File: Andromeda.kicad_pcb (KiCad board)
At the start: 2 copper layers, 30 parts, among them J1 Barrel_Jack, J2 USB_C_Receptacle_USB2.0, M1 Motor_DC, SW1 Reset, SW2 Boot, SW4 SW_DIP_x01, U1 ESP32-S2-SOLO, U2 DRV8871DDA, U3 AP2127K-3.3

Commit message: begin layout
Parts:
- removed C19: 47uF, Capacitor_SMD:C_0805_2012Metric
- removed D2: LED, Diode_SMD:D_1206_3216Metric
- removed M1: Motor_DC, Connector_Wire:SolderWire-0.75sqmm_1x02_P7mm_D1.25mm_OD3.5mm
- removed SW4: SW_DIP_x01, Connector_Wire:SolderWire-2.5sqmm_1x02_P7.2mm_D2.4mm_OD3.6mm
- added C10: 0.1uF, Capacitor_SMD:C_0805_2012Metric, F.Cu at (180.7, 137.0)
- added C11: 10uF, Capacitor_SMD:C_0805_2012Metric, F.Cu at (27.9, 24.1)
- added C12: 0.1uF, Capacitor_SMD:C_0805_2012Metric, F.Cu at (27.9, 30.0)
- added C13: 22uF, Capacitor_SMD:C_0805_2012Metric, F.Cu at (29.2, 38.1)
- added C14: 22uF, Capacitor_SMD:C_0805_2012Metric, F.Cu at (39.0, 44.5)
- added C15: 0.1uF, Capacitor_SMD:C_0805_2012Metric, F.Cu at (176.5, 102.2)
- added C16: 0.1uF, Capacitor_SMD:C_0805_2012Metric, F.Cu at (180.9, 102.2)
- added C18: 0.1uF, Capacitor_SMD:C_0805_2012Metric, F.Cu at (76.2, 189.2)
- added C7: 0.1uF, Capacitor_SMD:C_0805_2012Metric, F.Cu at (117.2, 174.0)
- added C8: 0.1uF, Capacitor_SMD:C_0805_2012Metric, F.Cu at (64.8, 177.8)
- added C9: 0.1uF, Capacitor_SMD:C_0805_2012Metric, F.Cu at (176.2, 137.0)
- added F2: Fuse_Small, Fuse:Fuse_0805_2012Metric, F.Cu at (180.0, 59.7)
- added J10: RJ45, Connector_RJ:RJ45_Amphenol_54602-x08_Horizontal, F.Cu at (238.7, 130.1)
- added J11: Conn_01x08_Pin, Connector_PinHeader_2.54mm:PinHeader_2x08_P2.54mm_Vertical, F.Cu at (16.3, 118.6)
- added J12: RJ45, Connector_RJ:RJ45_Amphenol_54602-x08_Horizontal, F.Cu at (238.7, 112.4)
- added J13: RJ45, Connector_RJ:RJ45_Amphenol_54602-x08_Horizontal, F.Cu at (238.7, 94.7)
- added J3: RJ45, Connector_RJ:RJ45_Amphenol_54602-x08_Horizontal, F.Cu at (167.6, 85.9)
- added J4: RJ45, Connector_RJ:RJ45_Amphenol_54602-x08_Horizontal, F.Cu at (167.6, 103.6)
- added J5: RJ45, Connector_RJ:RJ45_Amphenol_54602-x08_Horizontal, F.Cu at (167.6, 121.3)
- added J6: RJ45, Connector_RJ:RJ45_Amphenol_54602-x08_Horizontal, F.Cu at (167.6, 138.9)
- added J7: RJ45, Connector_RJ:RJ45_Amphenol_54602-x08_Horizontal, F.Cu at (210.8, 137.2)
- added J8: RJ45, Connector_RJ:RJ45_Amphenol_54602-x08_Horizontal, F.Cu at (191.0, 137.2)
- added J9: RJ45, Connector_RJ:RJ45_Amphenol_54602-x08_Horizontal, F.Cu at (238.7, 147.8)
- added L1: 4.7uH, Inductor_THT:L_Radial_D9.5mm_P5.00mm_Fastron_07HVP, F.Cu at (47.0, 34.3)
- added R10: 1K, Resistor_SMD:R_0805_2012Metric, F.Cu at (81.6, 172.7)
- added R11: 1K, Resistor_SMD:R_0805_2012Metric, F.Cu at (180.9, 106.0)
- added R14: 1K, Resistor_SMD:R_0805_2012Metric, F.Cu at (68.9, 185.4)
- added R15: 1K, Resistor_SMD:R_0805_2012Metric, F.Cu at (175.9, 146.1)
- added R16: 1K, Resistor_SMD:R_0805_2012Metric, F.Cu at (175.9, 148.6)
- added R17: 1K, Resistor_SMD:R_0805_2012Metric, F.Cu at (176.5, 112.4)
- added R18: 1K, Resistor_SMD:R_0805_2012Metric, F.Cu at (176.5, 114.9)
- added R19: 1K, Resistor_SMD:R_0805_2012Metric, F.Cu at (212.4, 128.9)
- added R20: 1K, Resistor_SMD:R_0805_2012Metric, F.Cu at (220.3, 129.5)
- added R21: 1K, Resistor_SMD:R_0805_2012Metric, F.Cu at (200.3, 129.5)
- added R22: 1K, Resistor_SMD:R_0805_2012Metric, F.Cu at (193.7, 128.9)
- added R23: 1K, Resistor_SMD:R_0805_2012Metric, F.Cu at (229.9, 142.2)
- added R24: 1K, Resistor_SMD:R_0805_2012Metric, F.Cu at (229.9, 137.8)
- added R25: 1K, Resistor_SMD:R_0805_2012Metric, F.Cu at (229.5, 125.1)
- added R26: 1K, Resistor_SMD:R_0805_2012Metric, F.Cu at (229.2, 120.0)
- added R27: 1K, Resistor_SMD:R_0805_2012Metric, F.Cu at (230.1, 104.1)
- added R28: 1K, Resistor_SMD:R_0805_2012Metric, F.Cu at (229.9, 108.6)
- added R29: 1K, Resistor_SMD:R_0805_2012Metric, F.Cu at (229.2, 90.2)
- added R30: 1K, Resistor_SMD:R_0805_2012Metric, F.Cu at (229.2, 85.1)
- added R31: 1K, Resistor_SMD:R_0805_2012Metric, F.Cu at (29.4, 115.6)
- added R32: 1K, Resistor_SMD:R_0805_2012Metric, F.Cu at (29.2, 123.2)
- added R33: 1K, Resistor_SMD:R_0805_2012Metric, F.Cu at (32.7, 140.1)
- added R34: 1K, Resistor_SMD:R_0805_2012Metric, F.Cu at (27.9, 132.1)
- added R5: 1K, Resistor_SMD:R_0805_2012Metric, F.Cu at (116.3, 179.1)
- added R6: 1K, Resistor_SMD:R_0805_2012Metric, F.Cu at (180.6, 140.9)
- added R7: 1K, Resistor_SMD:R_0805_2012Metric, F.Cu at (43.5, 22.9)
- added R8: 1K, Resistor_SMD:R_0805_2012Metric, F.Cu at (110.5, 171.4)
- added SW3: SW_Nidec_CAS-120A1, Button_Switch_SMD:Nidec_Copal_CAS-120A, F.Cu at (219.1, 43.8)
- added U4: DRV8212DSGR, DRV8870DDA:WSON_212DSGR_TEX, F.Cu at (176.3, 140.9)
- added U5: AP63205WU, Package_TO_SOT_SMD:TSOT-23-6, F.Cu at (36.8, 33.0)
- added U6: DRV8212DSGR, DRV8870DDA:WSON_212DSGR_TEX, F.Cu at (126.0, 175.8)
- added U7: DRV8212DSGR, DRV8870DDA:WSON_212DSGR_TEX, F.Cu at (78.7, 181.6)
- C2, C5: footprint Capacitor_SMD:C_0603_1608Metric -> Capacitor_SMD:C_0805_2012Metric
- R3: value 150 -> 1K; footprint Resistor_SMD:R_0603_1608Metric -> Resistor_SMD:R_0805_2012Metric
- R4: value 30k -> 1K
- R9: footprint Resistor_SMD:R_0603_1608Metric -> Resistor_SMD:R_0805_2012Metric
- U2: value DRV8871DDA -> DRV8212DSGR; footprint Package_SO:Texas_HTSOP-8-1EP_3.9x4.9mm_P1.27mm_EP2.95x4.9mm_Mask2.4x3.1mm_ThermalVias -> DRV8870DDA:WSON_212DSGR_TEX
- moved J1 123.3 mm to (242.8, 62.9), turned to 90 degrees
- moved R4 122.3 mm to (72.4, 174.0)
- moved U1 118.3 mm to (208.4, 90.6)
- moved D3 100.5 mm to (35.3, 72.4)
- moved TP2 97.8 mm to (21.0, 49.8)
- moved TP3 97.8 mm to (21.0, 55.9)
- moved C17 96.1 mm to (117.2, 167.6)
- moved F1 93.6 mm to (227.8, 43.8)
- moved R3 92.8 mm to (109.6, 177.8)
- moved R9 91.6 mm to (27.9, 72.4)
- moved C5 60.0 mm to (118.4, 22.9)
- moved C6 56.3 mm to (101.9, 21.6)
- moved D4 55.2 mm to (170.2, 59.7), turned to 180 degrees
- moved R2 54.0 mm to (84.2, 82.5)
- moved C1 50.8 mm to (82.5, 74.9)
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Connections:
- C17 pad 1: +12V -> +3.3V
- D4 pad 1: +5V -> Net-(D4-K)
- F1 pad 1: Net-(F1-Pad1) -> Net-(SW3-C)
- J1 pad 1: Net-(F1-Pad1) -> Net-(SW3-B)
- R3 pad 1: +5V -> Net-(U6-MODE)
- R3 pad 2: Net-(D2-A) -> GND
- R4 pad 1: Net-(U2-ILIM) -> Net-(U7-MODE)
- U1 pad 10: unconnected-(U1-GPIO17/U1TXD/ADC2_CH6/DAC_1-Pad10) -> GPIO17
- U1 pad 11: unconnected-(U1-GPIO18/U1RXD/ADC2_CH7/DAC_2/CLK_OUT3-Pad11) -> GPIO18
- U1 pad 12: unconnected-(U1-GPIO8/TOUCH8/ADC1_CH7-Pad12) -> GPIO8
- U1 pad 15: unconnected-(U1-GPIO3/TOUCH3/ADC1_CH2-Pad15) -> GPIO3
- U1 pad 22: unconnected-(U1-GPIO14/TOUCH14/ADC2_CH3/FSPIWP/FSPIDQS-Pad22) -> GPIO14
- U1 pad 26: unconnected-(U1-GPIO45-Pad26) -> GPIO45
- U1 pad 30: unconnected-(U1-SPIDQS/GPIO37/FSPIQ-Pad30) -> GPIO37
- U1 pad 31: unconnected-(U1-GPIO38/FSPIWP-Pad31) -> GPIO38
- U1 pad 32: unconnected-(U1-MTCK/GPIO39/CLK_OUT3-Pad32) -> GPIO39
- U1 pad 33: unconnected-(U1-MTDO/GPIO40/CLK_OUT2-Pad33) -> GPIO40
- U1 pad 34: unconnected-(U1-MTDI/GPIO41/CLK_OUT1-Pad34) -> GPIO41
- U1 pad 35: unconnected-(U1-MTMS/GPIO42-Pad35) -> GPIO42
- U1 pad 36: unconnected-(U1-U0RXD/GPIO44/CLK_OUT2-Pad36) -> GPIO44
- U1 pad 37: unconnected-(U1-U0TXD/GPIO43/CLK_OUT1-Pad37) -> GPIO43
- U1 pad 38: unconnected-(U1-GPIO2/TOUCH2/ADC1_CH1-Pad38) -> GPIO2
- U1 pad 39: unconnected-(U1-GPIO1/TOUCH1/ADC1_CH0-Pad39) -> GPIO1
- U1 pad 5: unconnected-(U1-GPIO5/TOUCH5/ADC1_CH4-Pad5) -> GPIO5
- U1 pad 6: unconnected-(U1-GPIO6/TOUCH6/ADC1_CH5-Pad6) -> GPIO6
- U1 pad 7: unconnected-(U1-GPIO7/TOUCH7/ADC1_CH6-Pad7) -> GPIO7
- U1 pad 8: unconnected-(U1-GPIO15/U0RTS/ADC2_CH4/XTAL_32K_P-Pad8) -> GPIO15
- U1 pad 9: unconnected-(U1-GPIO16/U0CTS/ADC2_CH5/XTAL_32K_N-Pad9) -> GPIO16
- U2 pad 1: GND -> +6V
- U2 pad 2: GPIO36 -> Net-(U2-OUT1)
- U2 pad 3: GPIO35 -> Net-(U2-OUT2)
- U2 pad 4: Net-(U2-ILIM) -> GND
- U2 pad 5: +12V -> GPIO40
- U2 pad 6: Net-(U2-OUT1) -> GPIO39
- U2 pad 7: GND -> Net-(U2-MODE)
- U2 pad 8: Net-(M1--) -> +3.3V
- U2 pad 9: GND -> (no net)
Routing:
- net Net-(U4-OUT1): track 0.00 -> 9.44 mm
- net Net-(U2-OUT1): track 0.00 -> 9.02 mm
- net Net-(J4-Pad7): track 0.00 -> 8.48 mm
- net +3.3V: track 0.00 -> 8.42 mm
- net Net-(J6-Pad7): track 0.00 -> 7.55 mm
- net Net-(J4-Pad8): track 0.00 -> 6.46 mm
- net +6V: track 0.00 -> 6.40 mm
- net Net-(U2-OUT2): track 0.00 -> 6.16 mm
- net Net-(U4-OUT2): track 0.00 -> 5.86 mm
- net Net-(J6-Pad8): track 0.00 -> 5.12 mm
- net Net-(U2-MODE): track 0.00 -> 2.58 mm
- net Net-(U4-MODE): track 0.00 -> 2.54 mm
- added copper zone on B.Cu, net GND
- added copper zone on F.Cu, net GND
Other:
- board outline added: 101.6 x 101.6 mm

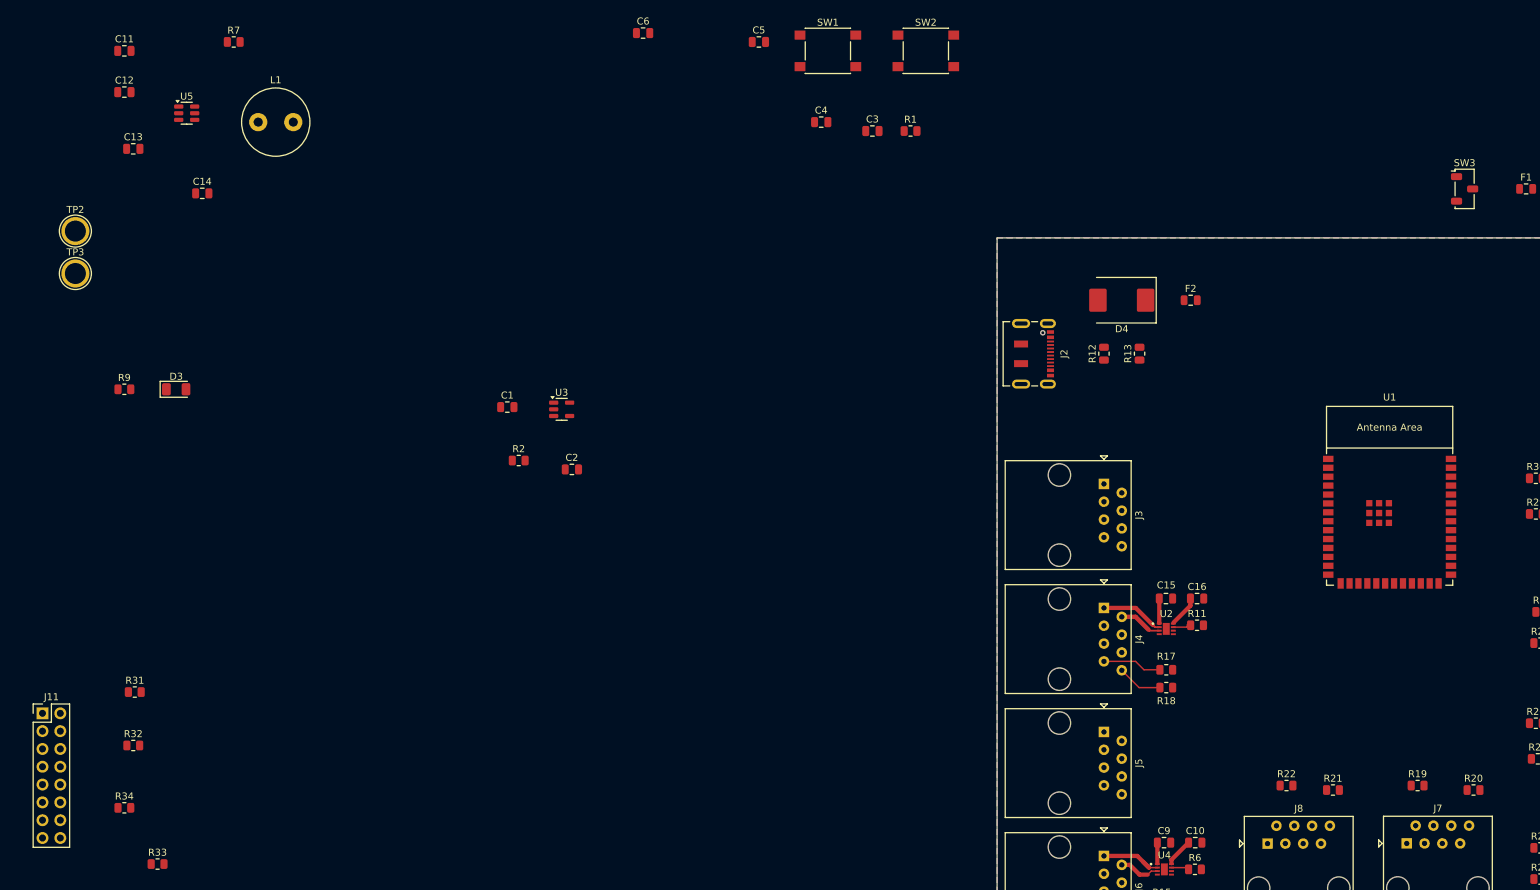
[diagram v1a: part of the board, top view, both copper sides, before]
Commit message: Switch to 5V, Add Gyro, GPIO extender
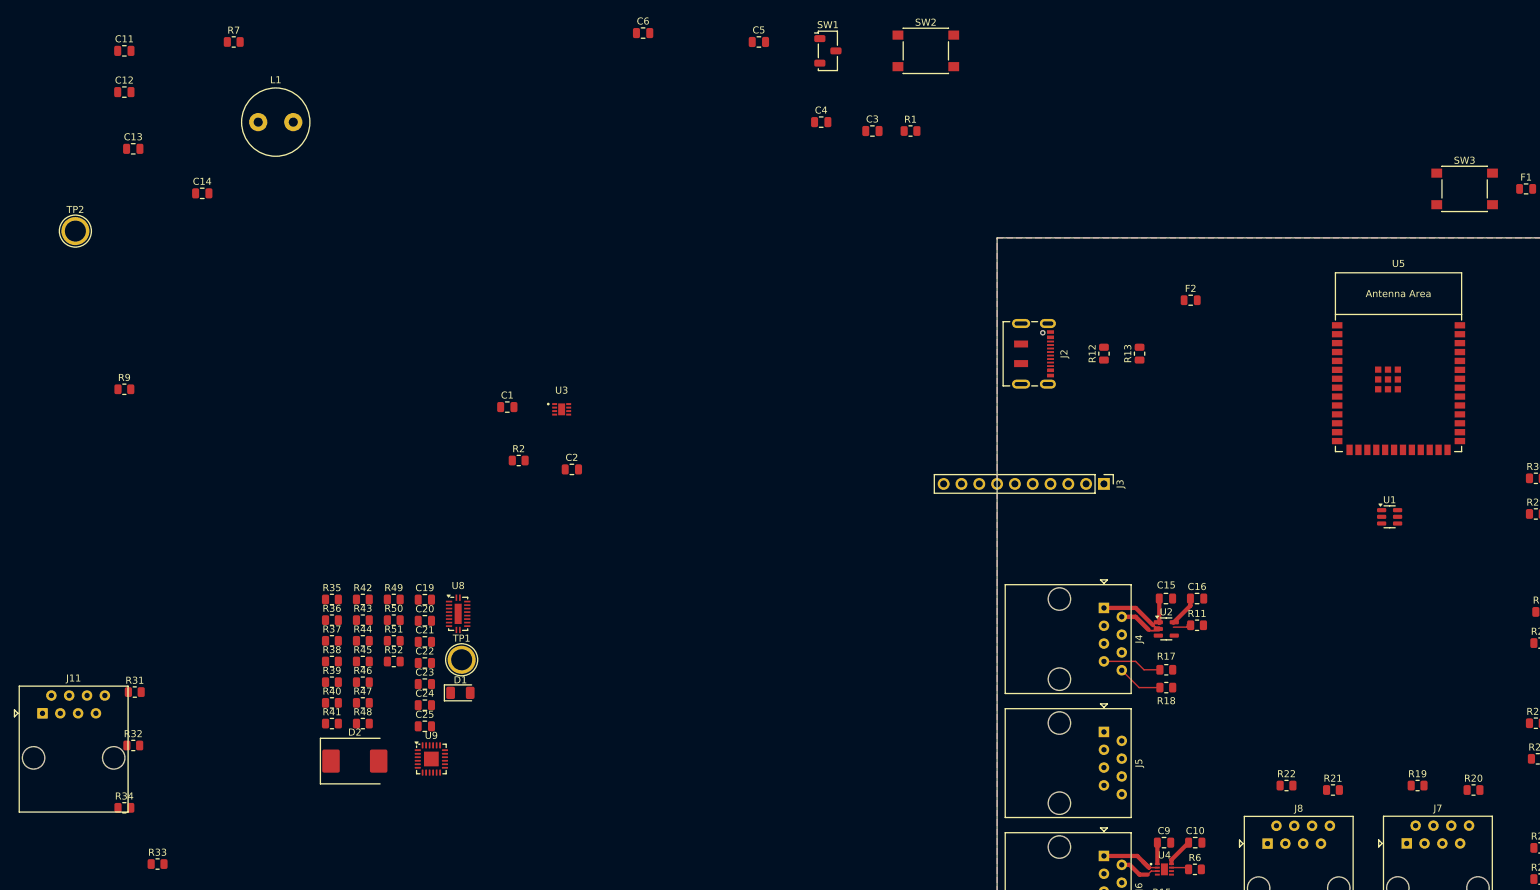
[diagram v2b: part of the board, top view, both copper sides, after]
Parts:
- removed D3: LED, Diode_SMD:D_1206_3216Metric
- removed D4: D_Schottky, Diode_SMD:D_SMC
- removed TP3: TestPoint, TestPoint:TestPoint_Plated_Hole_D3.0mm
- added C19: .1uF, Capacitor_SMD:C_0805_2012Metric, F.Cu at (70.8, 102.4)
- added C20: .1uF, Capacitor_SMD:C_0805_2012Metric, F.Cu at (70.8, 105.4)
- added C21: .1uF, Capacitor_SMD:C_0805_2012Metric, F.Cu at (70.8, 108.4)
- added C22: 10nF, Capacitor_SMD:C_0805_2012Metric, F.Cu at (70.8, 111.4)
- added C23: .1uF, Capacitor_SMD:C_0805_2012Metric, F.Cu at (70.8, 114.4)
- added C24: 0.1uF, Capacitor_SMD:C_0805_2012Metric, F.Cu at (70.8, 117.4)
- added C25: 2.2uF, Capacitor_SMD:C_0805_2012Metric, F.Cu at (70.8, 120.5)
- added D1: LED, Diode_SMD:D_1206_3216Metric, F.Cu at (75.9, 115.7)
- added D2: D_Schottky, Diode_SMD:D_SMC, F.Cu at (60.8, 125.4)
- added R35: 20K, Resistor_SMD:R_0805_2012Metric, F.Cu at (57.5, 102.4)
- added R36: 10K, Resistor_SMD:R_0805_2012Metric, F.Cu at (57.5, 105.3)
- added R37: 10K, Resistor_SMD:R_0805_2012Metric, F.Cu at (57.5, 108.3)
- added R38: 10K, Resistor_SMD:R_0805_2012Metric, F.Cu at (57.5, 111.2)
- added R39: 10K, Resistor_SMD:R_0805_2012Metric, F.Cu at (57.5, 114.2)
- added R40: 1K, Resistor_SMD:R_0805_2012Metric, F.Cu at (57.5, 117.1)
- added R41: 1K, Resistor_SMD:R_0805_2012Metric, F.Cu at (57.5, 120.1)
- added R42: 10K, Resistor_SMD:R_0805_2012Metric, F.Cu at (62.0, 102.4)
- added R43: 20K, Resistor_SMD:R_0805_2012Metric, F.Cu at (62.0, 105.3)
- added R44: 10K, Resistor_SMD:R_0805_2012Metric, F.Cu at (62.0, 108.3)
- added R45: 10K, Resistor_SMD:R_0805_2012Metric, F.Cu at (62.0, 111.2)
- added R46: 10K, Resistor_SMD:R_0805_2012Metric, F.Cu at (62.0, 114.2)
- added R47: 10K, Resistor_SMD:R_0805_2012Metric, F.Cu at (62.0, 117.1)
- added R48: 1K, Resistor_SMD:R_0805_2012Metric, F.Cu at (62.0, 120.1)
- added R49: 10K, Resistor_SMD:R_0805_2012Metric, F.Cu at (66.4, 102.4)
- added R50: 1K, Resistor_SMD:R_0805_2012Metric, F.Cu at (66.4, 105.3)
- added R51: 10K, Resistor_SMD:R_0805_2012Metric, F.Cu at (66.4, 108.3)
- added R52: 20K, Resistor_SMD:R_0805_2012Metric, F.Cu at (66.4, 111.2)
- added TP1: TestPoint, TestPoint:TestPoint_Plated_Hole_D3.0mm, F.Cu at (76.0, 111.0)
- added U8: FXMA108, Package_DFN_QFN:WQFN-20-1EP_2.5x4.5mm_P0.5mm_EP1x2.9mm, F.Cu at (75.5, 104.4)
- added U9: PCAL6416AHF, Package_DFN_QFN:HVQFN-24-1EP_4x4mm_P0.5mm_EP2.1x2.1mm, F.Cu at (71.7, 125.1)
- C1: value 1uF -> 10uF
- C10: value 0.1uF -> 1uF
- C11: value 10uF -> .1uF
- C13, C14: value 22uF -> 0.1uF
- C16, C7: value 0.1uF -> .1uF
- C3: value .1uF -> 1uF
- C4: value .1uF -> 0.1uF
- C5: value 1uF -> 22uF
- C6: value .1uF -> 22uF
- J11: value Conn_01x08_Pin -> RJ45; footprint Connector_PinHeader_2.54mm:PinHeader_2x08_P2.54mm_Vertical -> Connector_RJ:RJ45_Amphenol_54602-x08_Horizontal
- J3: value RJ45 -> Conn_01x10_Pin; footprint Connector_RJ:RJ45_Amphenol_54602-x08_Horizontal -> Connector_PinHeader_2.54mm:PinHeader_1x10_P2.54mm_Vertical
- R1: value 10k -> 60
- R12, R13: value 5.1k -> 1K
- R2: value 3M -> 1K
- R23, R25, R32, R34: value 1K -> 10K
- R24, R26, R33: value 1K -> 20K
- R3: value 1K -> 3M
- R4, R5: value 1K -> 5.1k
- R6: value 1K -> 10k
- R9: value 60 -> 1K
- SW1: value Reset -> SW_Nidec_CAS-120A1; footprint Button_Switch_SMD:SW_Push_1P1T_NO_6x6mm_H9.5mm -> Button_Switch_SMD:Nidec_Copal_CAS-120A
- SW2: value Boot -> Reset
- SW3: value SW_Nidec_CAS-120A1 -> Boot; footprint Button_Switch_SMD:Nidec_Copal_CAS-120A -> Button_Switch_SMD:SW_Push_1P1T_NO_6x6mm_H9.5mm
- U1: value ESP32-S2-SOLO -> AP63205WU; footprint PCM_Espressif:ESP32-S2-SOLO -> Package_TO_SOT_SMD:TSOT-23-6
- U2: value DRV8212DSGR -> AP2127K-3.3; footprint DRV8870DDA:WSON_212DSGR_TEX -> Package_TO_SOT_SMD:SOT-23-5
- U3: value AP2127K-3.3 -> DRV8212DSGR; footprint Package_TO_SOT_SMD:SOT-23-5 -> DRV8870DDA:WSON_212DSGR_TEX
- U5: value AP63205WU -> ESP32-S3-WROOM-1; footprint Package_TO_SOT_SMD:TSOT-23-6 -> PCM_Espressif:ESP32-S3-WROOM-1
- moved U5 177.1 mm to (209.7, 71.5)
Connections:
- C10 pad 1: +3.3V -> GND
- C10 pad 2: GND -> +3.3V
- C11 pad 1: +6V -> GND
- C11 pad 2: GND -> +3.3V
- C12 pad 1: Net-(U5-BST) -> +3.3V
- C12 pad 2: Net-(U5-SW) -> GND
- C13 pad 1: +5V -> +3.3V
- C14 pad 1: +5V -> +6V
- C16 pad 1: +3.3V -> Net-(U5-GPIO0/BOOT)
- C2 pad 1: +3.3V -> +6V
- C3 pad 1: GND -> +3.3V
- C3 pad 2: Net-(U1-EN) -> GND
- C4 pad 1: Net-(U1-GPIO0) -> Net-(U1-BST)
- C4 pad 2: GND -> Net-(U1-SW)
- C5 pad 1: GND -> +5V
- C5 pad 2: +3.3V -> GND
- C6 pad 1: GND -> +5V
- C6 pad 2: +3.3V -> GND
- C7 pad 1: +6V -> GND
- C7 pad 2: GND -> Net-(U5-EN)
- F1 pad 1: Net-(SW3-C) -> Net-(SW1-C)
- J10 pad 4: unconnected-(J10-Pad4) -> +5V
- J10 pad 5: +3.3V -> GND
- J10 pad 6: GND -> Net-(J10-Pad6)
- J11 pad 1: Net-(J11-Pin_1) -> unconnected-(J11-Pad1)
- J11 pad 2: Net-(J11-Pin_2) -> unconnected-(J11-Pad2)
- J11 pad 3: Net-(J11-Pin_3) -> unconnected-(J11-Pad3)
- J11 pad 4: Net-(J11-Pin_4) -> +5V
- J11 pad 5: +3.3V -> GND
- J11 pad 6: +3.3V -> Net-(J11-Pad6)
- J11 pad 7: +5V -> Net-(J11-Pad7)
- J11 pad 8: GND -> Net-(J11-Pad8)
- J12 pad 4: unconnected-(J12-Pad4) -> +5V
- J12 pad 5: +3.3V -> GND
- J12 pad 6: GND -> Net-(J12-Pad6)
- J13 pad 4: unconnected-(J13-Pad4) -> +5V
- J13 pad 5: +3.3V -> GND
- J13 pad 6: GND -> Net-(J13-Pad6)
- J3 pad 1: Net-(U6-OUT1) -> GPIO7
- J3 pad 2: Net-(U6-OUT2) -> GPIO8
- J3 pad 3: unconnected-(J3-Pad3) -> GPIO9
- J3 pad 4: +6V -> GPIO10
- J3 pad 5: +3.3V -> GPIO11
- J3 pad 6: GND -> GPIO12
- J3 pad 7: Net-(J3-Pad7) -> GPIO13
- J3 pad 8: Net-(J3-Pad8) -> GPIO14
- J4 pad 1: Net-(U2-OUT1) -> Net-(U3-OUT1)
- J4 pad 2: Net-(U2-OUT2) -> Net-(U3-OUT2)
- J4 pad 3: unconnected-(J4-Pad3) -> +6V
- J4 pad 4: +6V -> +5V
- J4 pad 5: +3.3V -> GND
- J4 pad 6: GND -> Net-(J4-Pad6)
- J4 pad 8: Net-(J4-Pad8) -> unconnected-(J4-Pad8)
- J5 pad 1: Net-(U7-OUT1) -> Net-(U4-OUT1)
- J5 pad 2: Net-(U7-OUT2) -> Net-(U4-OUT2)
- J5 pad 3: unconnected-(J5-Pad3) -> +6V
- J5 pad 4: +6V -> +5V
- J5 pad 5: +3.3V -> GND
- J5 pad 6: GND -> Net-(J5-Pad6)
- J5 pad 8: Net-(J5-Pad8) -> unconnected-(J5-Pad8)
- J6 pad 1: Net-(U4-OUT1) -> Net-(U6-OUT1)
- J6 pad 2: Net-(U4-OUT2) -> Net-(U6-OUT2)
- J6 pad 3: unconnected-(J6-Pad3) -> +6V
- J6 pad 4: +6V -> +5V
- J6 pad 5: +3.3V -> GND
- J6 pad 6: GND -> Net-(J6-Pad6)
- J6 pad 8: Net-(J6-Pad8) -> unconnected-(J6-Pad8)
- J7 pad 1: unconnected-(J7-Pad1) -> Net-(U7-OUT1)
- J7 pad 2: unconnected-(J7-Pad2) -> Net-(U7-OUT2)
- J7 pad 3: unconnected-(J7-Pad3) -> +6V
- J7 pad 4: unconnected-(J7-Pad4) -> +5V
- J7 pad 5: +3.3V -> GND
- J7 pad 6: GND -> Net-(J7-Pad6)
- J7 pad 8: Net-(J7-Pad8) -> unconnected-(J7-Pad8)
- J8 pad 4: unconnected-(J8-Pad4) -> +5V
- J8 pad 5: +3.3V -> GND
- J8 pad 6: GND -> Net-(J8-Pad6)
- J9 pad 4: unconnected-(J9-Pad4) -> +5V
- J9 pad 5: +3.3V -> GND
- J9 pad 6: GND -> Net-(J9-Pad6)
- L1 pad 1: Net-(U5-BST) -> Net-(U1-BST)
- R1 pad 2: Net-(U1-EN) -> Net-(D1-A)
- R10 pad 2: GPIO34 -> ENC3B
- R11 pad 1: Net-(U2-MODE) -> Net-(U3-MODE)
- R12 pad 1: Net-(J2-CC2) -> Net-(U4-MODE)
- R13 pad 1: Net-(J2-CC1) -> Net-(J6-Pad6)
- R13 pad 2: GND -> ENC2A
- R14 pad 1: Net-(J5-Pad8) -> Net-(J6-Pad7)
- R14 pad 2: GPIO35 -> ENC2B
- R15 pad 1: Net-(J6-Pad7) -> Net-(J7-Pad6)
- R15 pad 2: GPIO36 -> ENC4A
- R16 pad 1: Net-(J6-Pad8) -> Net-(J7-Pad7)
- R16 pad 2: GPIO45 -> ENC4B
- R17 pad 1: Net-(J4-Pad7) -> Net-(J8-Pad6)
- R17 pad 2: GPIO21 -> EXP10
- R18 pad 1: Net-(J4-Pad8) -> Net-(J8-Pad7)
- R18 pad 2: GPIO33 -> EXP11
- R19 pad 1: Net-(J7-Pad7) -> Net-(U6-MODE)
- R19 pad 2: GPIO1 -> GND
- R2 pad 1: GND -> +6V
- R2 pad 2: Net-(U3-EN) -> Net-(U1-EN)
- R20 pad 1: Net-(J7-Pad8) -> Net-(U7-MODE)
- R20 pad 2: GPIO2 -> GND
- R21 pad 1: Net-(J8-Pad7) -> Net-(J9-Pad6)
- R21 pad 2: GPIO3 -> B0
- R22 pad 1: Net-(J8-Pad8) -> Net-(J9-Pad7)
- R22 pad 2: GPIO4 -> B1
- R23 pad 1: Net-(J9-Pad7) -> Net-(J8-Pad8)
- R24 pad 1: Net-(J9-Pad8) -> GPIO5
- R24 pad 2: GPIO6 -> GND
- R25 pad 1: Net-(J10-Pad7) -> Net-(J9-Pad8)
- R25 pad 2: GPIO7 -> GPIO1
- R26 pad 1: Net-(J10-Pad8) -> GPIO1
- R26 pad 2: GPIO8 -> GND
- R27 pad 1: Net-(J12-Pad7) -> Net-(J11-Pad6)
- R27 pad 2: GPIO9 -> EXP12
- R28 pad 1: Net-(J12-Pad8) -> Net-(J10-Pad6)
- R28 pad 2: GPIO10 -> B2
- R29 pad 1: Net-(J13-Pad7) -> Net-(J11-Pad7)
- R29 pad 2: GPIO11 -> EXP13
- R3 pad 1: Net-(U6-MODE) -> GND
- R3 pad 2: GND -> Net-(U2-EN)
- R30 pad 1: Net-(J13-Pad8) -> Net-(J10-Pad7)
- R30 pad 2: GPIO12 -> B3
- R31 pad 1: GPIO13 -> Net-(U8-~{OE})
- R31 pad 2: Net-(J11-Pin_1) -> GND
- R32 pad 1: GPIO14 -> Net-(J10-Pad8)
- R32 pad 2: Net-(J11-Pin_2) -> GPIO2
- R33 pad 1: GPIO15 -> GPIO2
- R33 pad 2: Net-(J11-Pin_3) -> GND
- R34 pad 1: GPIO16 -> Net-(J11-Pad8)
- R34 pad 2: Net-(J11-Pin_4) -> GPIO6
- R4 pad 1: Net-(U7-MODE) -> Net-(J2-CC2)
- R5 pad 1: Net-(J3-Pad7) -> Net-(J2-CC1)
- R5 pad 2: GPIO17 -> GND
- R6 pad 1: Net-(U4-MODE) -> +3.3V
- R6 pad 2: GND -> Net-(U5-EN)
- R7 pad 1: +6V -> Net-(J4-Pad6)
- R7 pad 2: Net-(U5-EN) -> ENC1A
- R8 pad 1: Net-(J3-Pad8) -> Net-(J4-Pad7)
- R8 pad 2: GPIO18 -> ENC1B
- R9 pad 1: +3.3V -> Net-(J5-Pad6)
- R9 pad 2: Net-(D3-A) -> ENC3A
- SW1 pad 1: GND -> Net-(SW1-C)
- SW1 pad 2: Net-(U1-EN) -> Net-(SW1-B)
- SW2 pad 1: Net-(U1-GPIO0) -> GND
- SW2 pad 2: GND -> Net-(U5-EN)
- SW3 pad 1: Net-(SW3-C) -> Net-(U5-GPIO0/BOOT)
- SW3 pad 2: Net-(SW3-B) -> GND
- TP2 pad 1: GND -> +6V
- U1 pad 1: GND -> +5V
- U1 pad 2: +3.3V -> Net-(U1-EN)
- U1 pad 3: Net-(U1-EN) -> +6V
- U1 pad 4: GPIO4 -> GND
- U1 pad 5: GPIO5 -> Net-(U1-SW)
- U1 pad 6: GPIO6 -> Net-(U1-BST)
- U2 pad 2: Net-(U2-OUT1) -> GND
- U2 pad 3: Net-(U2-OUT2) -> Net-(U2-EN)
- U2 pad 4: GND -> unconnected-(U2-NC-Pad4)
- U2 pad 5: GPIO40 -> +3.3V
- U3 pad 2: GND -> Net-(U3-OUT1)
- U3 pad 3: Net-(U3-EN) -> Net-(U3-OUT2)
- U3 pad 4: unconnected-(U3-NC-Pad4) -> GND
- U3 pad 5: +3.3V -> GPIO42
- U4 pad 5: GPIO44 -> GPIO46
- U4 pad 6: GPIO43 -> GPIO45
- U5 pad 1: +5V -> GND
- U5 pad 2: Net-(U5-EN) -> +3.3V
- U5 pad 3: +6V -> Net-(U5-EN)
- U5 pad 4: GND -> GPIO4
- U5 pad 5: Net-(U5-SW) -> GPIO5
- U5 pad 6: Net-(U5-BST) -> GPIO6
- U6 pad 5: GPIO38 -> GPIO44
- U6 pad 6: GPIO37 -> GPIO43
- U7 pad 5: GPIO42 -> GPIO48
- U7 pad 6: GPIO41 -> GPIO47
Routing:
- net Net-(J8-Pad7): track 0.00 -> 6.46 mm
- net Net-(J4-Pad8): track 6.46 -> 0.00 mm
- net Net-(J7-Pad7): track 0.00 -> 5.12 mm
- net Net-(J6-Pad8): track 5.12 -> 0.00 mm
- net Net-(U3-MODE): track 0.00 -> 2.58 mm
- net Net-(U2-MODE): track 2.58 -> 0.00 mm
